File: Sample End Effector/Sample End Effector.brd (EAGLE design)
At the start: 50.8 x 50.8 mm, 24 parts, among them IC1 LM2936MP-3.0, IC2 LM2936MP-3.0, U2 XBEE-1B3

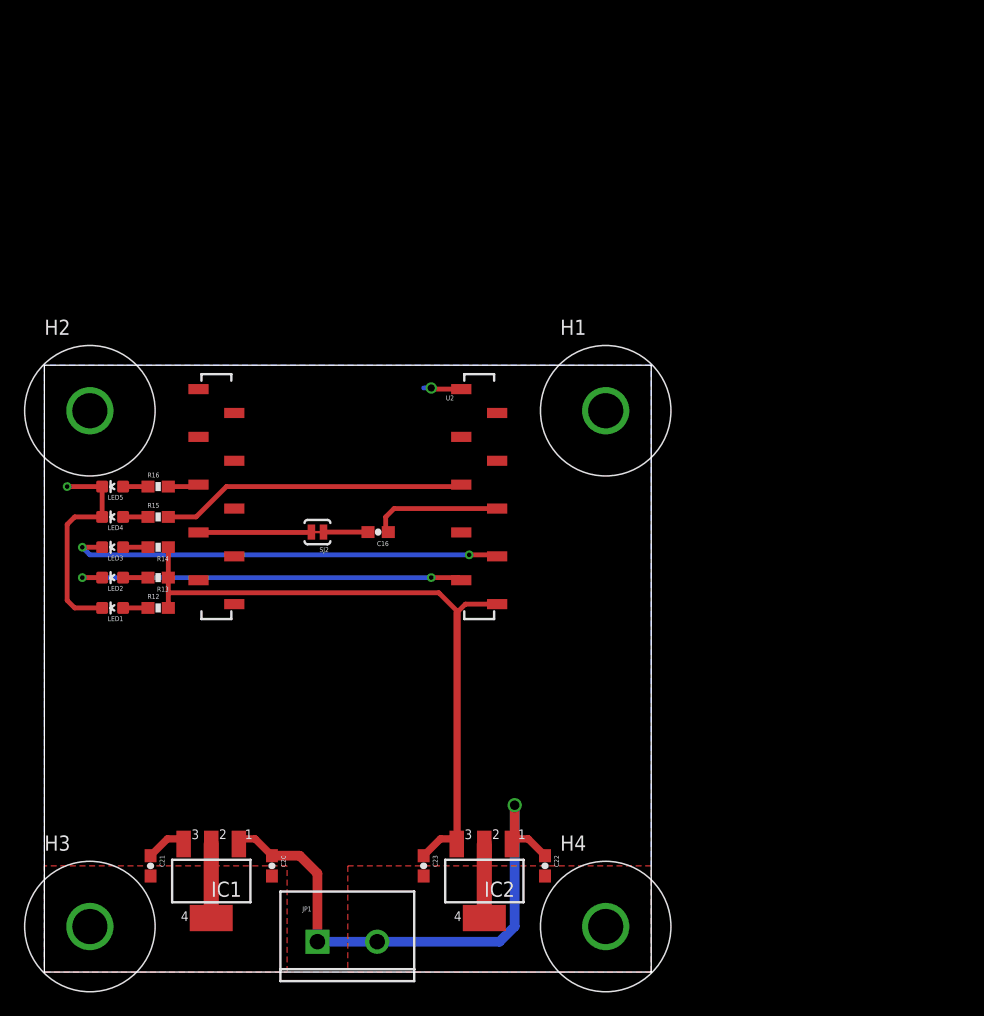
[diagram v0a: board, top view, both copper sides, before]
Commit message: Completed the new Sample End Effecter
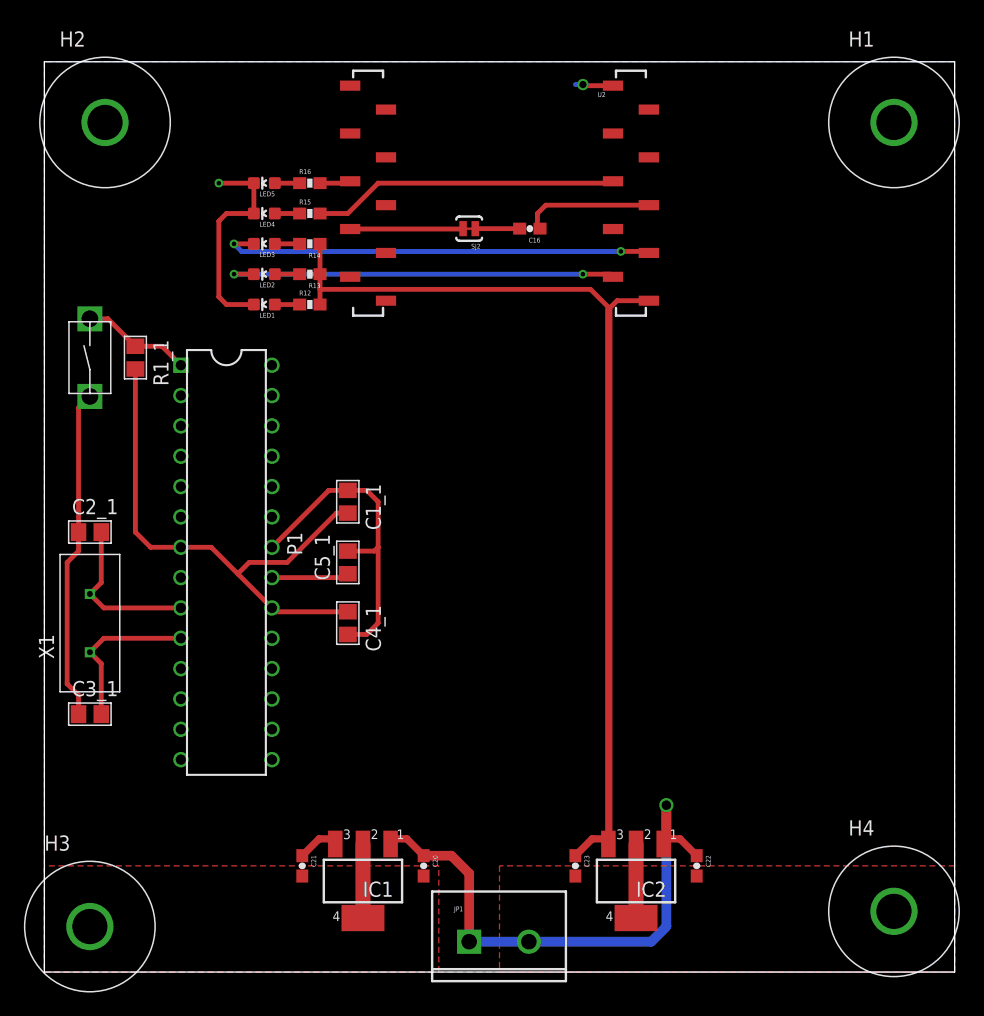
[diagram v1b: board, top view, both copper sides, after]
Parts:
- added C1_1, C4_1, C5_1: .1uF, Lib_Passive:C_0805
- added C2_1, C3_1: 15pF, Lib_Passive:C_0805
- added P1: ATMEGA328P, PCB0M1:DIP28
- added R1_1: 200, Lib_Passive:R_0805
- added S1: J_MC32857, PCB0M1:J_TOGGLE
- added X1: HC49S, PCB0M1:HC-49
- moved H1 34.1 mm to (71.1, 71.1)
- moved R16 28.4 mm to (22.2, 66.0)
- moved U2 28.4 mm to (38.1, 76.2)
- moved LED1 28.4 mm to (18.4, 55.9)
- moved R12 28.4 mm to (22.2, 55.9)
- moved LED5 28.4 mm to (18.4, 66.0)
- moved C16 28.4 mm to (40.6, 62.2)
- moved LED2 28.4 mm to (18.4, 58.4)
- moved LED3 28.4 mm to (18.4, 61.0)
- moved LED4 28.4 mm to (18.4, 63.5)
- moved R13 28.4 mm to (22.2, 58.4)
- moved R14 28.4 mm to (22.2, 61.0)
- moved R15 28.4 mm to (22.2, 63.5)
- moved SJ2 28.4 mm to (35.6, 62.2)
- moved H2 24.2 mm to (5.08, 71.1)
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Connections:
- new net BLANK1: P1.17
- new net D1: P1.3
- new net EN1: P1.19
- new net EXTMODE1: P1.16
- new net INTERRUPT1_1: P1.5
- new net INTERRUPT2_1: P1.4
- new net ISENSE1: P1.26
- new net LED1_1: P1.12
- new net LED2_1: P1.13
- new net N$1: C3_1.2, P1.10, X1.P$1
- new net N$12: C2_1.2, P1.9, X1.P$2
- new net N$14: C5_1.1, P1.21
- new net N$15: P1.1, R1_1.1, S1.P$2
- new net PFD1_1: P1.14
- new net PFD2_1: P1.18
- new net PHASE1: P1.23
- new net PULSE1: P1.11
- new net R1: P1.2
- new net REF1_1: P1.15
- new net SCL: P1.28
- new net SDA: P1.27
- new net SLEEP1_1: P1.24
- new net V5: C1_1.2, C4_1.1, P1.20, P1.7, R1_1.2
- net GND: now also C1_1.1, C2_1.1, C3_1.1, C4_1.2, C5_1.2, P1.22, P1.8, S1.P$1
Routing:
- net GND: track 33.4 -> 88.0 mm
- net V5: track 0.00 -> 45.5 mm
- net +3V3: track 56.8 -> 82.2 mm
- net N$1: track 0.00 -> 13.7 mm
- net N$12: track 0.00 -> 13.7 mm
- net N$15: track 0.00 -> 9.23 mm
- net N$14: track 0.00 -> 6.48 mm
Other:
- board size 50.8 x 50.8 mm -> 76.2 x 76.2 mm

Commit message: Finished sample end effecter and closes #4
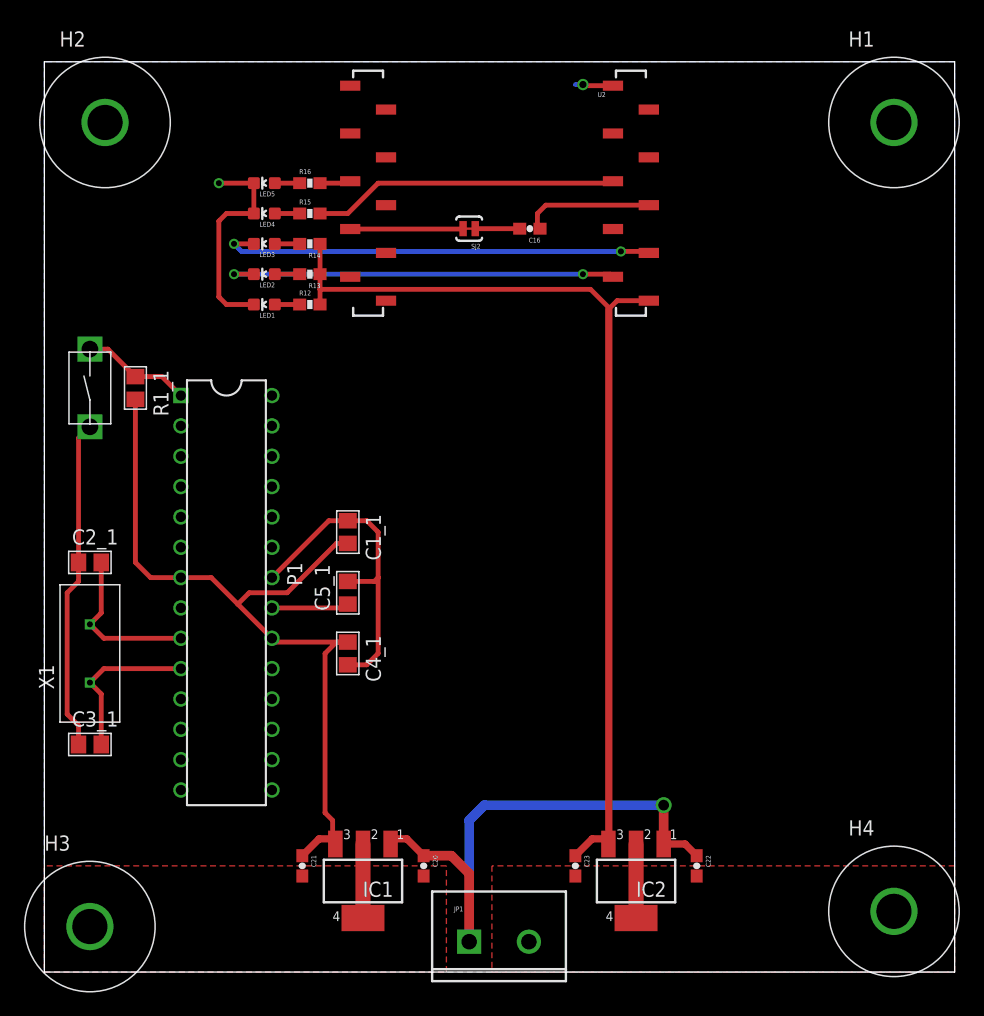
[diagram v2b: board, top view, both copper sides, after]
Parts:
- moved C1_1 2.54 mm to (25.4, 36.8)
- moved C2_1 2.54 mm to (3.81, 34.3)
- moved C3_1 2.54 mm to (3.81, 19.1)
- moved C4_1 2.54 mm to (25.4, 26.7)
- moved C5_1 2.54 mm to (25.4, 31.8)
- moved P1 2.54 mm to (15.2, 31.8)
- moved R1_1 2.54 mm to (7.62, 48.9)
- moved S1 2.54 mm to (3.81, 48.9)
- moved X1 2.54 mm to (3.81, 26.7)
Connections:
- removed net V5: C1_1.2, C4_1.1, P1.20, P1.7, R1_1.2
- net +5V: now also C1_1.2, C4_1.1, P1.20, P1.7, R1_1.2
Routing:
- net +5V: track 3.53 -> 67.2 mm
- net V5: track 45.5 -> 0.00 mm
